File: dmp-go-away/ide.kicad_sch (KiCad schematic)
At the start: 5 parts, among them J2 Conn_02x20_Odd_Even, U7 74LS245, U8 74LS245

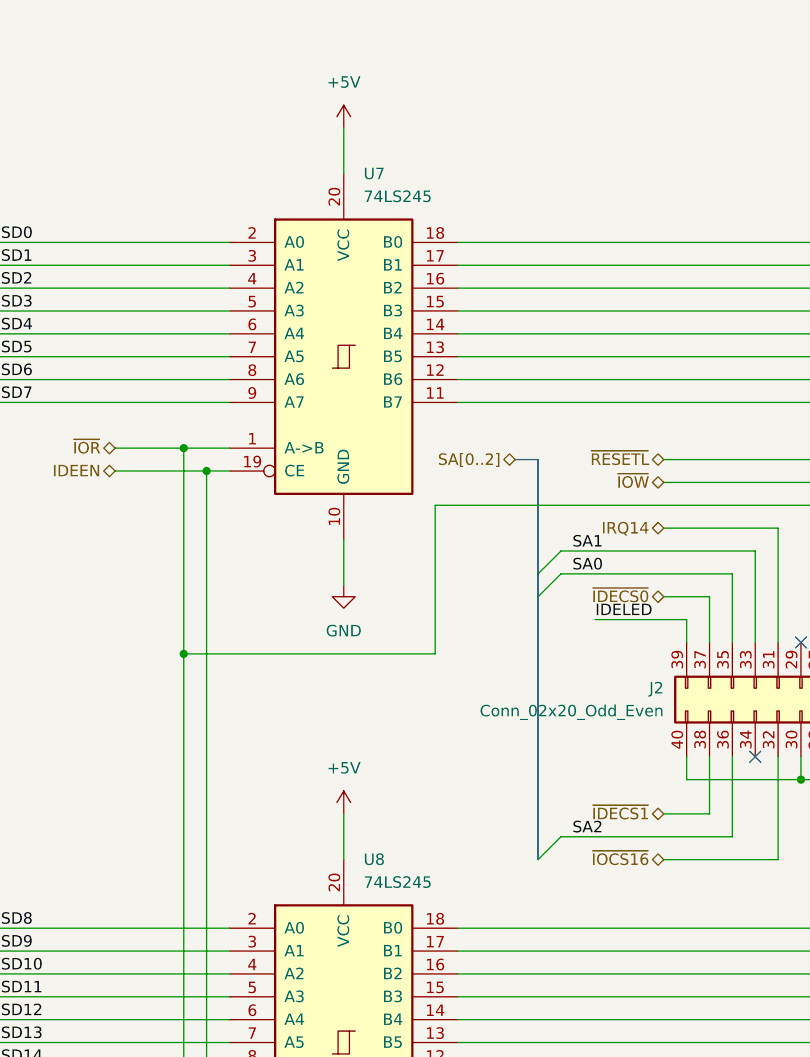
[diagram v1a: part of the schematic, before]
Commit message: Adding IDE fixes and some layout work
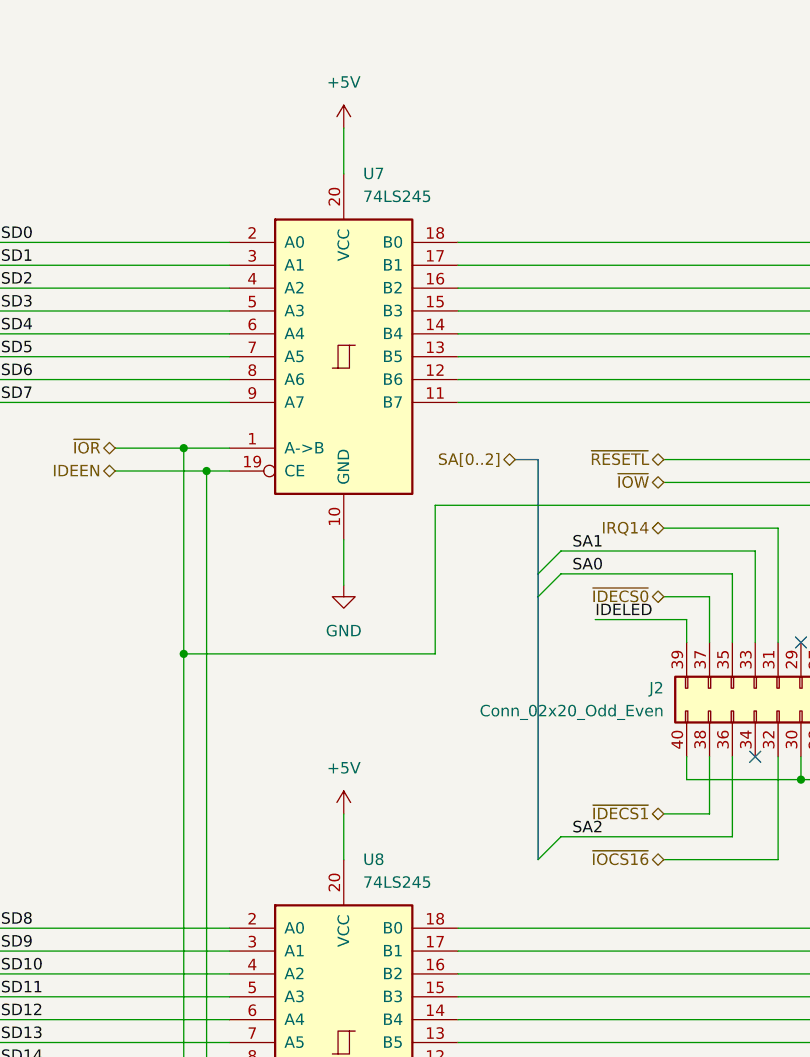
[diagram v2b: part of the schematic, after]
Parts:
- U7, U8: footprint Package_SO:SSOP-20_5.3x7.2mm_P0.65mm -> Package_SO:SOIC-20W_7.5x12.8mm_P1.27mm
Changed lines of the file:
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@@
 		(fields_autoplaced yes)
 		(property "Reference" "U8"
-			(at 129.1941 132.08 0)
+			(at 129.1433 132.08 0)
 			(effects
 				(font
@@
 		)
 		(property "Value" "74LS245"
-			(at 129.1941 134.62 0)
+			(at 129.1433 134.62 0)
 			(effects
 				(font
@@
 			)
 		)
-		(property "Footprint" "Package_SO:SSOP-20_5.3x7.2mm_P0.65mm"
+		(property "Footprint" "Package_SO:SOIC-20W_7.5x12.8mm_P1.27mm"
 			(at 127 152.4 0)
 			(effects
@@
 		(fields_autoplaced yes)
 		(property "Reference" "U7"
-			(at 129.1941 55.88 0)
+			(at 129.1433 55.88 0)
 			(effects
 				(font
@@
 		)
 		(property "Value" "74LS245"
-			(at 129.1941 58.42 0)
+			(at 129.1433 58.42 0)
 			(effects
 				(font
@@
 			)
 		)
-		(property "Footprint" "Package_SO:SSOP-20_5.3x7.2mm_P0.65mm"
+		(property "Footprint" "Package_SO:SOIC-20W_7.5x12.8mm_P1.27mm"
 			(at 127 76.2 0)
 			(effects
